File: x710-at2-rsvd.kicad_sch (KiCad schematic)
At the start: 37 parts, among them J7 PinHeader_1x3_P2.54mm_Drill1.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, U4 EZX710AT2_S_LMR5

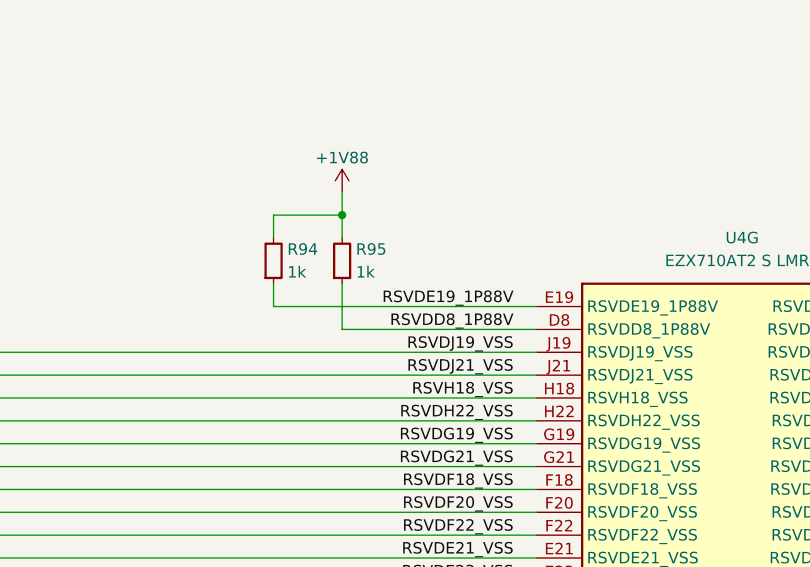
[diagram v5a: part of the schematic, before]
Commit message: [#80813] Adjust passives values, add remaining decoupling capacitors
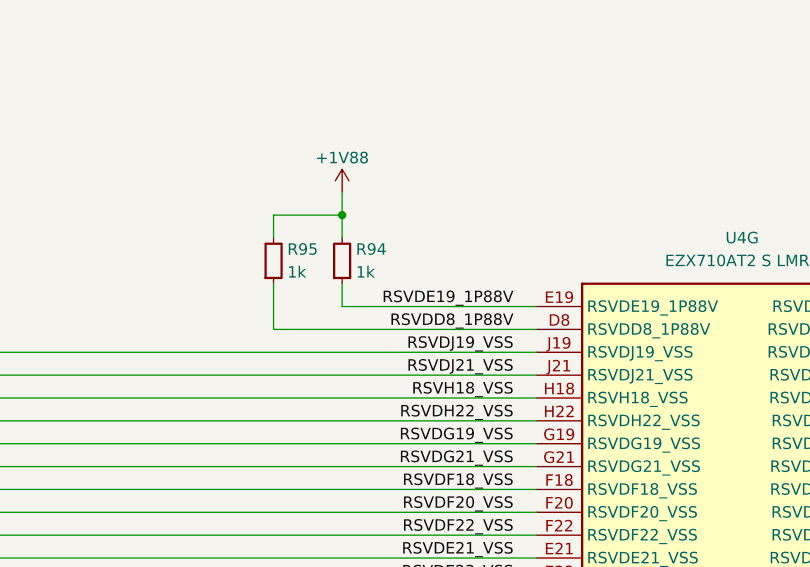
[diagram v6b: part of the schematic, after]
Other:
- moved on the sheet: R94, R95
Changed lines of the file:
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@@
 	)
 	(junction
-		(at 173.99 168.91)
+		(at 276.86 39.37)
 		(diameter 0)
 		(color 0 0 0 0)
 	)
 	(junction
-		(at 276.86 39.37)
+		(at 276.86 49.53)
 		(diameter 0)
 		(color 0 0 0 0)
 	)
 	(junction
-		(at 276.86 49.53)
+		(at 269.24 52.07)
 		(diameter 0)
 		(color 0 0 0 0)
 	)
 	(junction
-		(at 269.24 52.07)
+		(at 173.99 168.91)
 		(diameter 0)
 		(color 0 0 0 0)
@@
 	(wire
 		(pts
-			(xy 166.37 168.91) (xy 166.37 171.45)
+			(xy 173.99 168.91) (xy 173.99 171.45)
 		)
 		(stroke
@@
 	(wire
 		(pts
-			(xy 166.37 168.91) (xy 173.99 168.91)
-		)
-		(stroke
-			(width 0)
-			(type default)
-		)
-	)
-	(wire
-		(pts
 			(xy 144.78 247.65) (xy 144.78 250.19)
 		)
@@
 	(wire
 		(pts
-			(xy 173.99 168.91) (xy 173.99 171.45)
+			(xy 166.37 168.91) (xy 166.37 171.45)
 		)
 		(stroke
@@
 	(wire
 		(pts
-			(xy 166.37 176.53) (xy 166.37 179.07)
+			(xy 173.99 176.53) (xy 173.99 179.07)
 		)
 		(stroke
@@
 	(wire
 		(pts
-			(xy 173.99 176.53) (xy 173.99 181.61)
+			(xy 166.37 176.53) (xy 166.37 181.61)
 		)
 		(stroke
@@
 	(wire
 		(pts
-			(xy 166.37 179.07) (xy 195.58 179.07)
+			(xy 173.99 179.07) (xy 195.58 179.07)
 		)
 		(stroke
@@
 	(wire
 		(pts
-			(xy 173.99 181.61) (xy 195.58 181.61)
+			(xy 166.37 181.61) (xy 195.58 181.61)
 		)
 		(stroke
@@
 	(wire
 		(pts
+			(xy 166.37 168.91) (xy 173.99 168.91)
+		)
+		(stroke
+			(width 0)
+			(type default)
+		)
+	)
+	(wire
+		(pts
 			(xy 109.22 199.39) (xy 109.22 242.57)
 		)
@@
 	(symbol
 		(lib_id "antmicroResistors0402:R_1k_0402")
-		(at 173.99 176.53 90)
+		(at 166.37 176.53 90)
 		(unit 1)
 		(exclude_from_sim no)
@@
 		(dnp no)
 		(property "Reference" "R95"
-			(at 175.514 172.72 90)
+			(at 167.894 172.72 90)
 			(effects
 				(font
@@
 		)
 		(property "Value" "R_1k_0402"
-			(at 186.69 156.21 0)
+			(at 179.07 156.21 0)
 			(effects
 				(font
@@
 		)
 		(property "Footprint" "antmicro-footprints:R_0402_1005Metric"
-			(at 189.23 156.21 0)
+			(at 181.61 156.21 0)
 			(effects
 				(font
@@
 		)
 		(property "Datasheet" "https://www.bourns.com/docs/product-datasheets/cr.pdf"
-			(at 191.77 156.21 0)
+			(at 184.15 156.21 0)
 			(effects
 				(font
@@
 		)
 		(property "Description" "SMD Chip Resistor, 1 kohm, ± 1%, 63 mW, 0402 [1005 Metric], Thick Film, General Purpose"
-			(at 173.99 176.53 0)
+			(at 166.37 176.53 0)
 			(effects
 				(font
@@
 		)
 		(property "MPN" "CR0402-FX-1001GLF"
-			(at 194.31 156.21 0)
+			(at 186.69 156.21 0)
 			(effects
 				(font
@@
 		)
 		(property "Manufacturer" "Bourns"
-			(at 196.85 156.21 0)
+			(at 189.23 156.21 0)
 			(effects
 				(font
@@
 		)
 		(property "License" "Apache-2.0"
-			(at 199.39 156.21 0)
+			(at 191.77 156.21 0)
 			(effects
 				(font
@@
 		)
 		(property "Author" "Antmicro"
-			(at 201.93 156.21 0)
+			(at 194.31 156.21 0)
 			(effects
 				(font
@@
 		)
 		(property "Val" "1k"
-			(at 175.514 175.26 90)
+			(at 167.894 175.26 90)
 			(effects
 				(font
@@
 		)
 		(property "Tolerance" "1%"
-			(at 184.15 156.21 0)
+			(at 176.53 156.21 0)
 			(effects
 				(font
@@
 	(symbol
 		(lib_id "antmicroResistors0402:R_1k_0402")
-		(at 166.37 176.53 90)
+		(at 173.99 176.53 90)
 		(unit 1)
 		(exclude_from_sim no)
@@
 		(dnp no)
 		(property "Reference" "R94"
-			(at 167.894 172.72 90)
+			(at 175.514 172.72 90)
 			(effects
 				(font
@@
 		)
 		(property "Value" "R_1k_0402"
-			(at 179.07 156.21 0)
+			(at 186.69 156.21 0)
 			(effects
 				(font
@@
 		)
 		(property "Footprint" "antmicro-footprints:R_0402_1005Metric"
-			(at 181.61 156.21 0)
+			(at 189.23 156.21 0)
 			(effects
 				(font
@@
 		)
 		(property "Datasheet" "https://www.bourns.com/docs/product-datasheets/cr.pdf"
-			(at 184.15 156.21 0)
+			(at 191.77 156.21 0)
 			(effects
 				(font
@@
 		)
 		(property "Description" "SMD Chip Resistor, 1 kohm, ± 1%, 63 mW, 0402 [1005 Metric], Thick Film, General Purpose"
-			(at 166.37 176.53 0)
+			(at 173.99 176.53 0)
 			(effects
 				(font
@@
 		)
 		(property "MPN" "CR0402-FX-1001GLF"
-			(at 186.69 156.21 0)
+			(at 194.31 156.21 0)
 			(effects
 				(font
@@
 		)
 		(property "Manufacturer" "Bourns"
-			(at 189.23 156.21 0)
+			(at 196.85 156.21 0)
 			(effects
 				(font
@@
 		)
 		(property "License" "Apache-2.0"
-			(at 191.77 156.21 0)
+			(at 199.39 156.21 0)
 			(effects
 				(font
@@
 		)
 		(property "Author" "Antmicro"
-			(at 194.31 156.21 0)
+			(at 201.93 156.21 0)
 			(effects
 				(font
@@
 		)
 		(property "Val" "1k"
-			(at 167.894 175.26 90)
+			(at 175.514 175.26 90)
 			(effects
 				(font
@@
 		)
 		(property "Tolerance" "1%"
-			(at 176.53 156.21 0)
+			(at 184.15 156.21 0)
 			(effects
 				(font
@@
 	)
 	(symbol
-		(lib_name "EZX710AT2_S_LMR5_1")
 		(lib_id "antmicroInterfaceControllers:EZX710AT2_S_LMR5")
 		(at 195.58 49.53 0)
@@
 		(pin "U37"
 		)
-		(pin "M31"
-		)
 		(pin "AC7"
 		)
@@
 		(pin "J13"
 		)
-		(pin "M15"
+		(pin "V34"
 		)
 		(pin "M10"

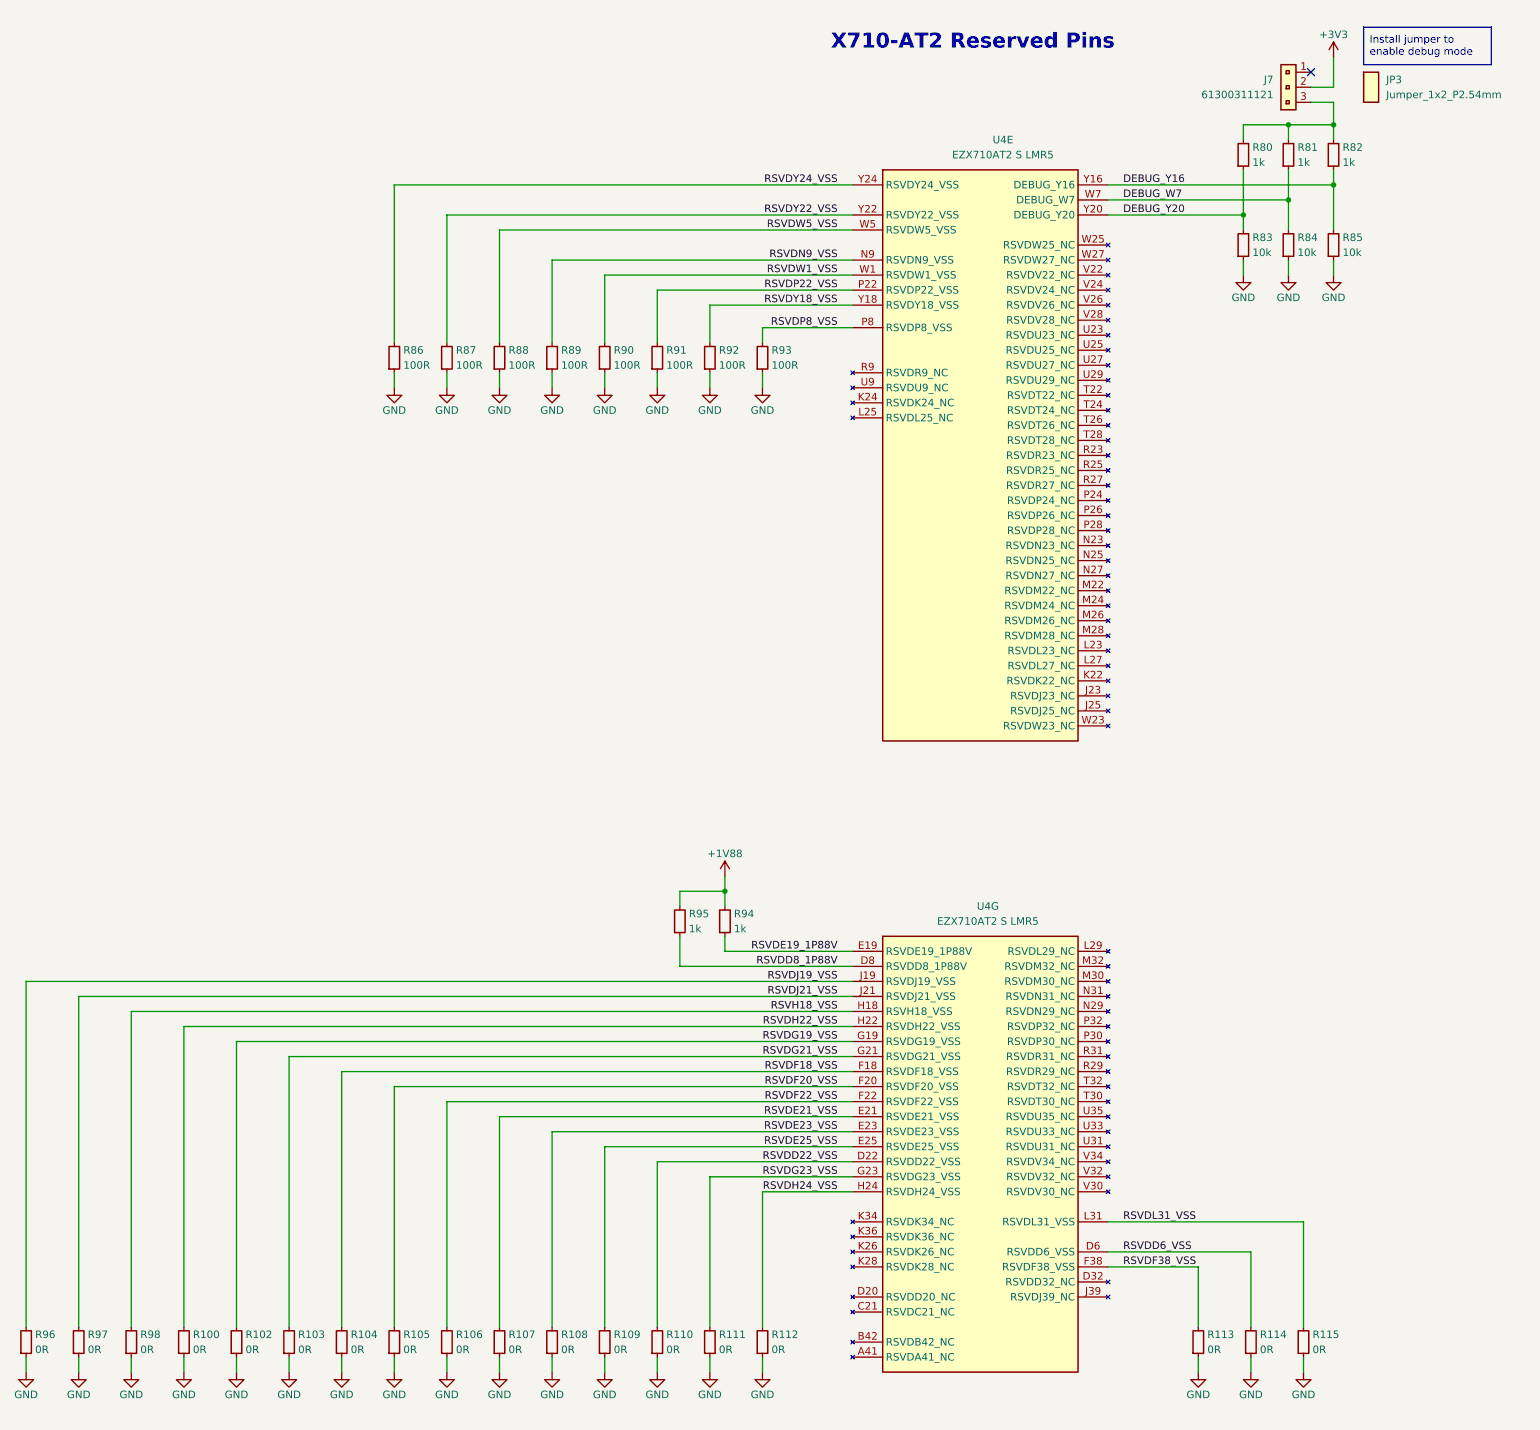
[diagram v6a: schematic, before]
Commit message: [#80813] Add OCuLink connector
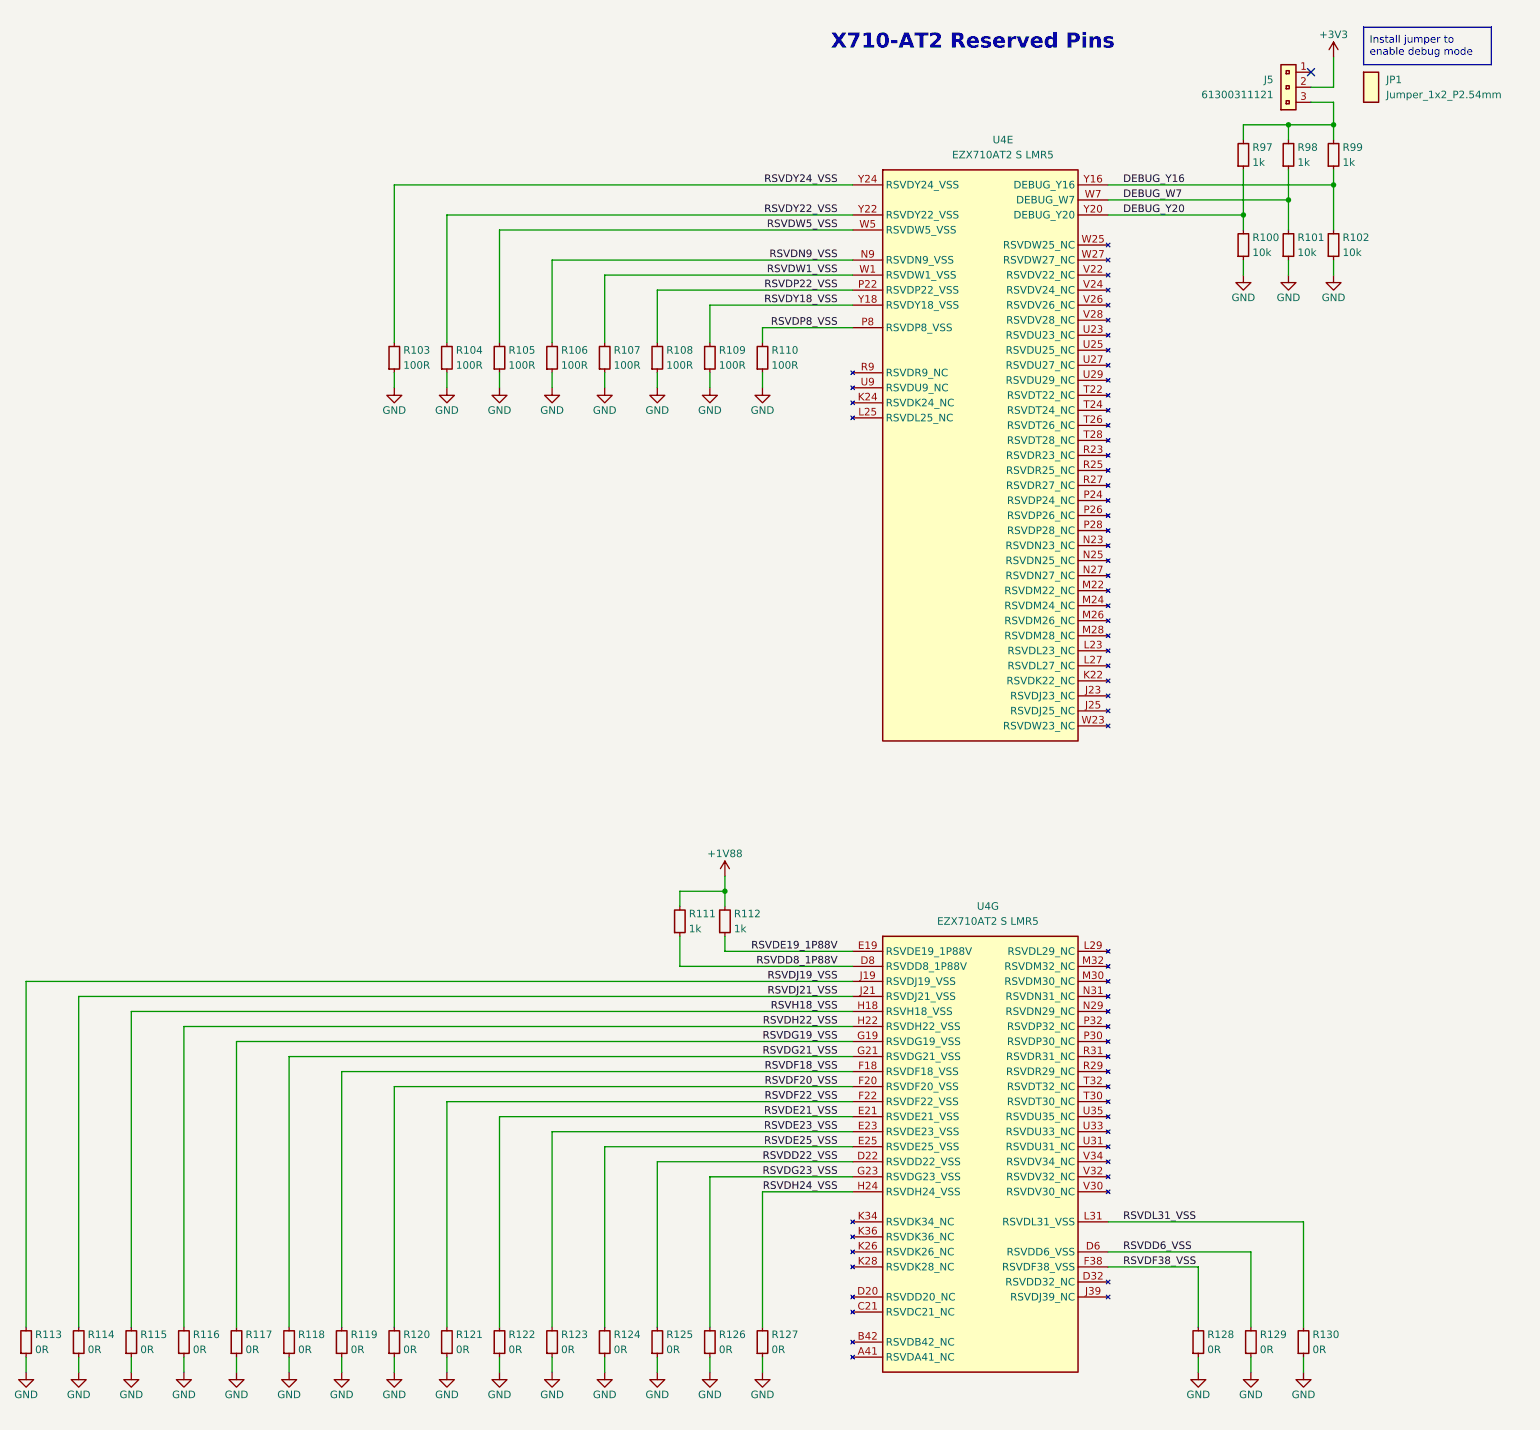
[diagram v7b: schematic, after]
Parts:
- renumbered J7 to J5, JP3 to JP1, R83 to R100, R84 to R101, R85 to R102, R86 to R103, R87 to R104, R88 to R105, R89 to R106, R90 to R107, R91 to R108, R92 to R109, R93 to R110, R95 to R111, R94 to R112, R96 to R113, R97 to R114, R98 to R115, R100 to R116, R102 to R117, R103 to R118, R104 to R119, R105 to R120, R106 to R121, R107 to R122, R108 to R123, R109 to R124, R110 to R125, R111 to R126, R112 to R127, R113 to R128, R114 to R129, R115 to R130, R80 to R97, R81 to R98, R82 to R99

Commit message: [#81595] Update symbols from library
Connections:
- no-connect marks 1 -> 64
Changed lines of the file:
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@@
 	)
 	(no_connect
+		(at 238.76 212.09)
+	)
+	(no_connect
+		(at 238.76 135.89)
+	)
+	(no_connect
+		(at 238.76 237.49)
+	)
+	(no_connect
+		(at 195.58 88.9)
+	)
+	(no_connect
+		(at 195.58 81.28)
+	)
+	(no_connect
+		(at 238.76 120.65)
+	)
+	(no_connect
+		(at 238.76 110.49)
+	)
+	(no_connect
+		(at 238.76 62.23)
+	)
+	(no_connect
+		(at 238.76 214.63)
+	)
+	(no_connect
+		(at 238.76 118.11)
+	)
+	(no_connect
+		(at 238.76 97.79)
+	)
+	(no_connect
+		(at 195.58 86.36)
+	)
+	(no_connect
+		(at 238.76 67.31)
+	)
+	(no_connect
+		(at 195.58 245.11)
+	)
+	(no_connect
+		(at 238.76 77.47)
+	)
+	(no_connect
+		(at 195.58 229.87)
+	)
+	(no_connect
+		(at 238.76 125.73)
+	)
+	(no_connect
+		(at 238.76 105.41)
+	)
+	(no_connect
+		(at 195.58 227.33)
+	)
+	(no_connect
+		(at 238.76 140.97)
+	)
+	(no_connect
+		(at 238.76 69.85)
+	)
+	(no_connect
+		(at 195.58 240.03)
+	)
+	(no_connect
+		(at 238.76 113.03)
+	)
+	(no_connect
+		(at 238.76 123.19)
+	)
+	(no_connect
+		(at 238.76 92.71)
+	)
+	(no_connect
+		(at 238.76 59.69)
+	)
+	(no_connect
+		(at 238.76 85.09)
+	)
+	(no_connect
+		(at 238.76 95.25)
+	)
+	(no_connect
+		(at 238.76 64.77)
+	)
+	(no_connect
+		(at 195.58 237.49)
+	)
+	(no_connect
+		(at 195.58 224.79)
+	)
+	(no_connect
+		(at 238.76 196.85)
+	)
+	(no_connect
+		(at 238.76 219.71)
+	)
+	(no_connect
+		(at 238.76 87.63)
+	)
+	(no_connect
+		(at 238.76 207.01)
+	)
+	(no_connect
+		(at 238.76 82.55)
+	)
+	(no_connect
+		(at 238.76 74.93)
+	)
+	(no_connect
+		(at 238.76 199.39)
+	)
+	(no_connect
+		(at 238.76 72.39)
+	)
+	(no_connect
+		(at 238.76 181.61)
+	)
+	(no_connect
+		(at 238.76 179.07)
+	)
+	(no_connect
+		(at 238.76 184.15)
+	)
+	(no_connect
+		(at 238.76 191.77)
+	)
+	(no_connect
+		(at 195.58 83.82)
+	)
+	(no_connect
+		(at 238.76 100.33)
+	)
+	(no_connect
+		(at 195.58 232.41)
+	)
+	(no_connect
+		(at 238.76 194.31)
+	)
+	(no_connect
+		(at 238.76 209.55)
+	)
+	(no_connect
+		(at 238.76 128.27)
+	)
+	(no_connect
+		(at 238.76 133.35)
+	)
+	(no_connect
+		(at 238.76 115.57)
+	)
+	(no_connect
 		(at 273.05 30.48)
 	)
+	(no_connect
+		(at 238.76 102.87)
+	)
+	(no_connect
+		(at 238.76 234.95)
+	)
+	(no_connect
+		(at 238.76 201.93)
+	)
+	(no_connect
+		(at 238.76 130.81)
+	)
+	(no_connect
+		(at 238.76 189.23)
+	)
+	(no_connect
+		(at 238.76 80.01)
+	)
+	(no_connect
+		(at 238.76 90.17)
+	)
+	(no_connect
+		(at 238.76 107.95)
+	)
+	(no_connect
+		(at 238.76 204.47)
+	)
+	(no_connect
+		(at 238.76 138.43)
+	)
+	(no_connect
+		(at 238.76 217.17)
+	)
+	(no_connect
+		(at 238.76 186.69)
+	)
 	(wire
 		(pts
@@
 			)
 		)
-		(property "Description" ""
+		(property "Description" "Jumper"
 			(at 281.94 30.48 0)
 			(effects
@@
 			)
 		)
-		(property "Description" ""
+		(property "Description" "Pin Header, Vertical, Board-to-Board, 2.54 mm, 1 Rows, 3 Contacts, Through Hole Straight, WR-PHD"
 			(at 273.05 30.48 0)
 			(effects
